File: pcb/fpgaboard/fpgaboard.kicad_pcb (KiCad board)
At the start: 4 copper layers, 140 x 140 mm, 342 parts, among them J1 CONN_02X02, J10 CONN_02X05, J11 Micro_SD_Card_Det_Hirose_DM3AT, J12 CONN_02X16, J13 CONN_02X16, J14 CONN_02X03, J15 GB_CARTRIDGE_CONN, J16 CONN_02X16, J17 CONN_02X16, J18 CONN_02X16, J19 CONN_02X03, J2 MICRO_USB, J20 CONN_02X05, J21 CONN_02X03, J22 CONN_02X05, J23 CONN_02X03, J24 CONN_02X03, J25 GBC_ELP, J26 CONN_02X05, J27 CONN_02X03, J28 SJ1-3533NG, J3 CONN_02X03, J4 CONN_01X02, J5 CONN_02X03, J6 CONN_01X21, J7 CONN_02X05, J8 CONN_02X05, J9 CONN_02X03, Q1 BSS138, Q2 BSS138, SW0 SW_Push, SW1 SW_Push, SW2 SW_Push, SW3 SW_Push, SW4 SW_DIP_x08, SW5 SW_DIP_x08, U1 LT3030EFE#TRPBF, U10 74LVCH8T245, U11 74LVCH8T245, U12 74LVCH8T245, U13 74LVCH8T245, U14 74LVCH8T245, U15 74LVCH8T245, U16 74LVCH8T245, U17 IS62WV1288BLL-55QLI, U18 IS62WV10248EBLL-45TLI, U19 74AHC1GU04, U2 W25Q32JVSSIM, U20 IS62WV1288BLL-55QLI, U21 IS62WV10248EBLL-45TLI, U22 IS62WV1288BLL-55QLI, U23 TDA7050, U24 TDA7050, U3 iCE40-HX8K-CT256, U4 93LC56B, U5 FT2232H, U6 74LVCH8T245, U7 74LVCH8T245, U8 74LVCH8T245, U9 74LVCH8T245, X1 12M, X2 16.777216M

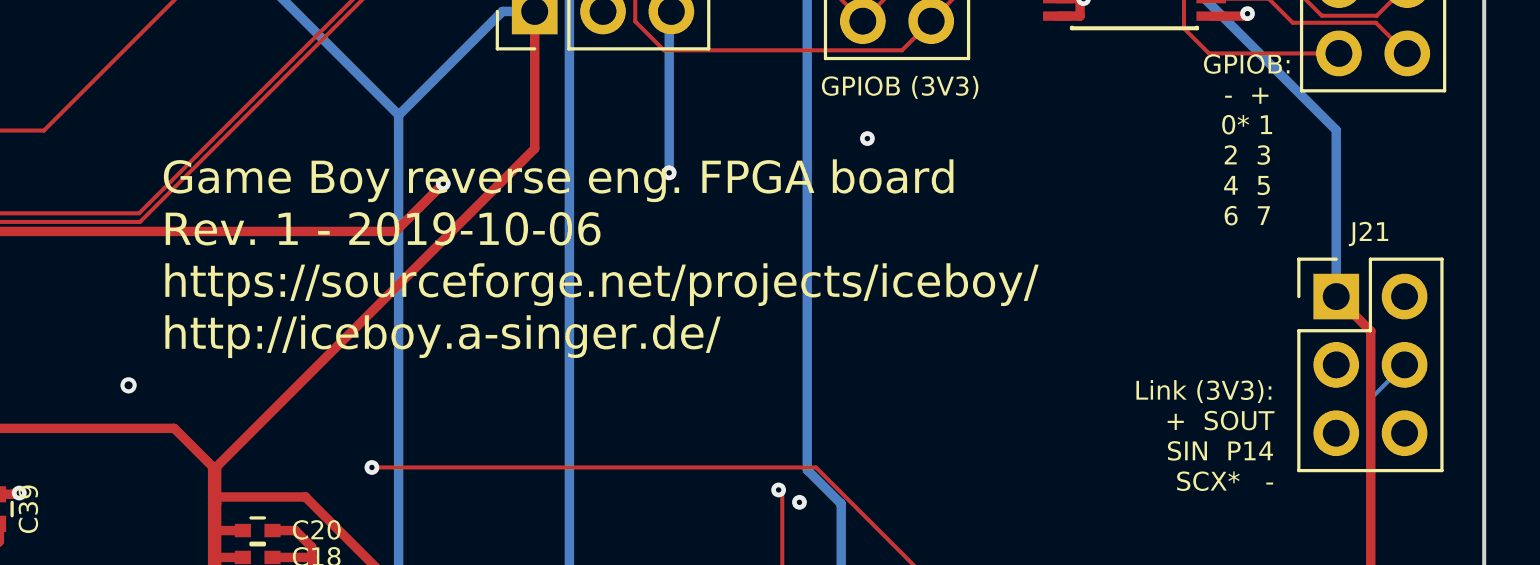
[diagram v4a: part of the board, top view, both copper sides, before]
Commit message: Update page infos of fpgaboard KiCad files
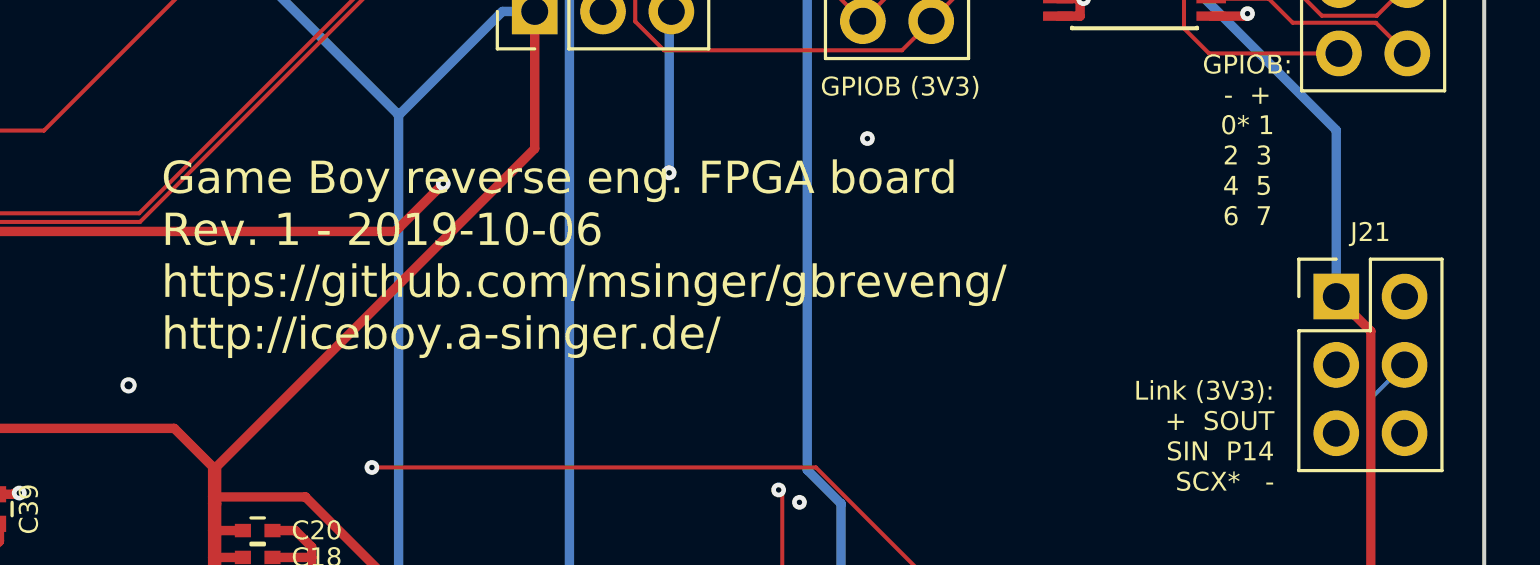
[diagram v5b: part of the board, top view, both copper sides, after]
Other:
- board text added: "Game Boy reverse eng. FPGA board Rev. 1 - 2019-10-06 https://github.com/msinger/gbreveng/ http://iceboy.a-singer.de/"
- board text removed: "Game Boy reverse eng. FPGA board Rev. 1 - 2019-10-06 https://sourceforge.net/projects/iceboy/ http://iceboy.a-singer.de/"
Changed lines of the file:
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@@
     (date 2020-08-29)
     (rev 1)
-    (company "Author: Michael Singer")
+    (company "CC-BY-SA-4.0 Michael Singer")
     (comment 1 https://sourceforge.net/projects/iceboy/)
-    (comment 2 http://iceboy.a-singer.de/)
+    (comment 2 https://github.com/msinger/gbreveng/)
+    (comment 3 http://iceboy.a-singer.de/)
   )
   (layers
@@
   )
   (setup
-    (last_trace_width 0.5)
+    (last_trace_width 0.15)
     (user_trace_width 0.1016)
     (user_trace_width 0.15)
@@
   (gr_line (start 129.92 65.74) (end 124 65.74) (angle 90) (layer F.SilkS) (width 0.2))
   (gr_arc (start 129.91 67.82) (end 129.91 65.75) (angle 90) (layer F.SilkS) (width 0.2))
-  (gr_text "Game Boy reverse eng. FPGA board\nRev. 1 - 2019-10-06\nhttps://sourceforge.net/projects/iceboy/\nhttp://iceboy.a-singer.de/" (at 140.82 126.59) (layer F.SilkS)
+  (gr_text "Game Boy reverse eng. FPGA board\nRev. 1 - 2019-10-06\nhttps://github.com/msinger/gbreveng/\nhttp://iceboy.a-singer.de/" (at 140.82 126.59) (layer F.SilkS)
     (effects (font (size 1.2 1.2) (thickness 0.2)) (justify left))
   )
